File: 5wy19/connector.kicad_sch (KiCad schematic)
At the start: 1 part, among them J1 Conn_02x41_Row_Letter_First_S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

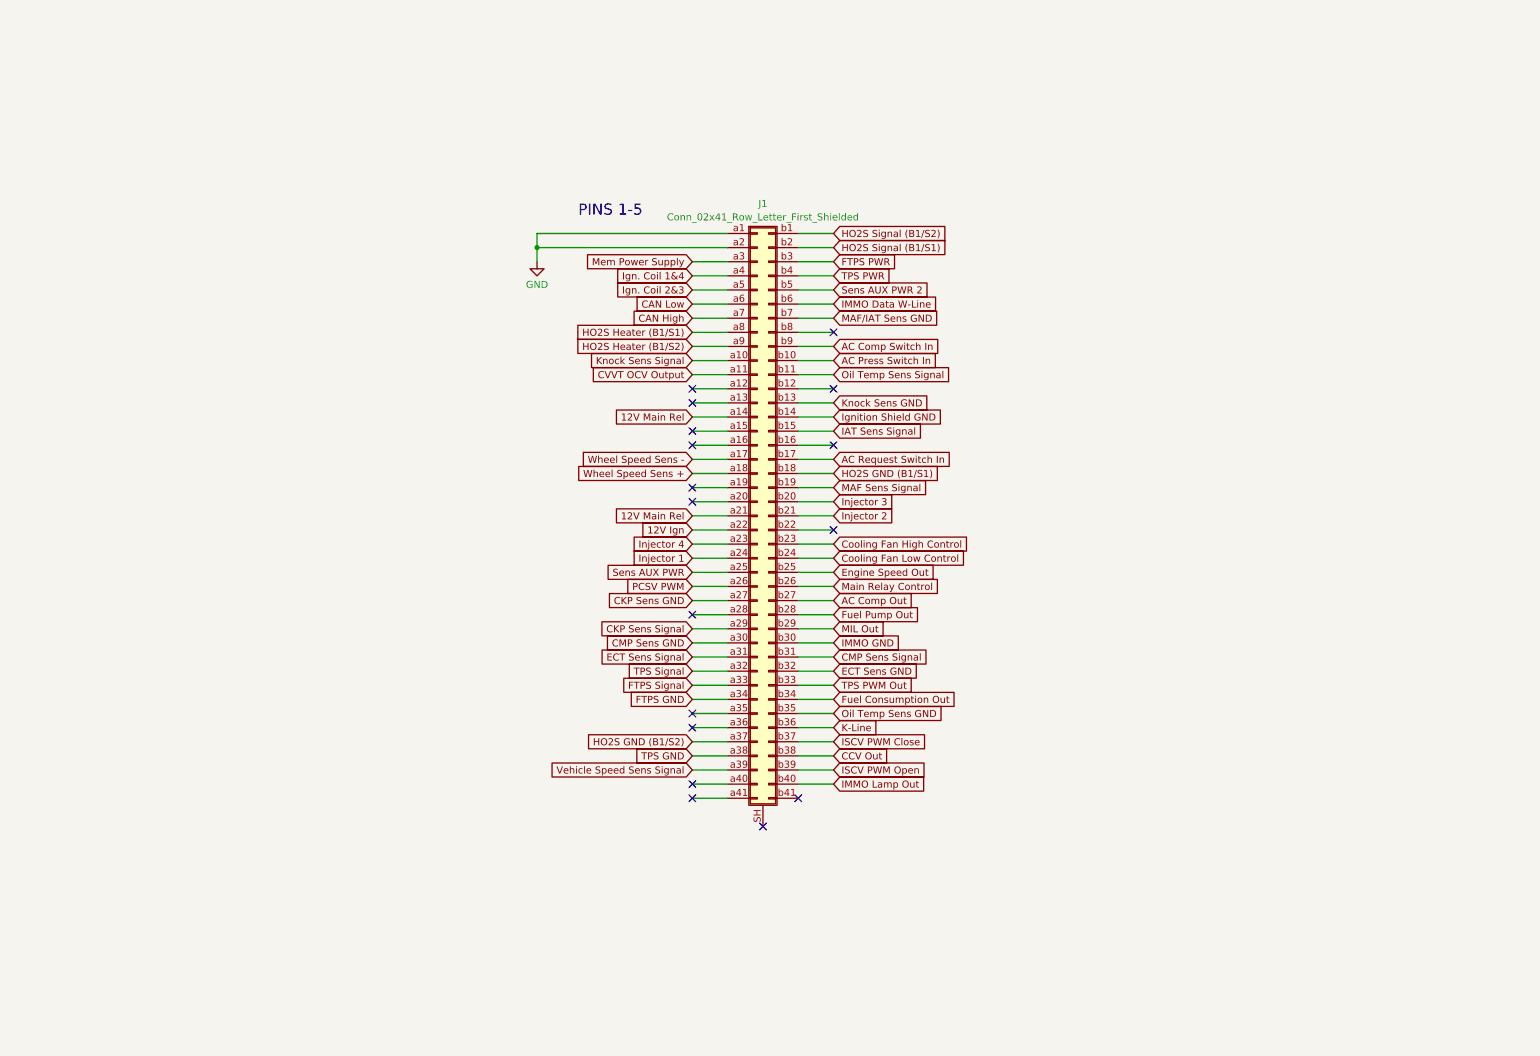
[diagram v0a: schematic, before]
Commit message: Finished most of the subsystems
-- MCU finished
-- Flash finished
-- Power Supply finished
-- I/O Drivers finished
-- CANBUS finished
-- Knock Control finished
-- Connector finished
-- Ignition Driver finished
-- Sensor Logic mostly finished
-- Logic ICs need some work
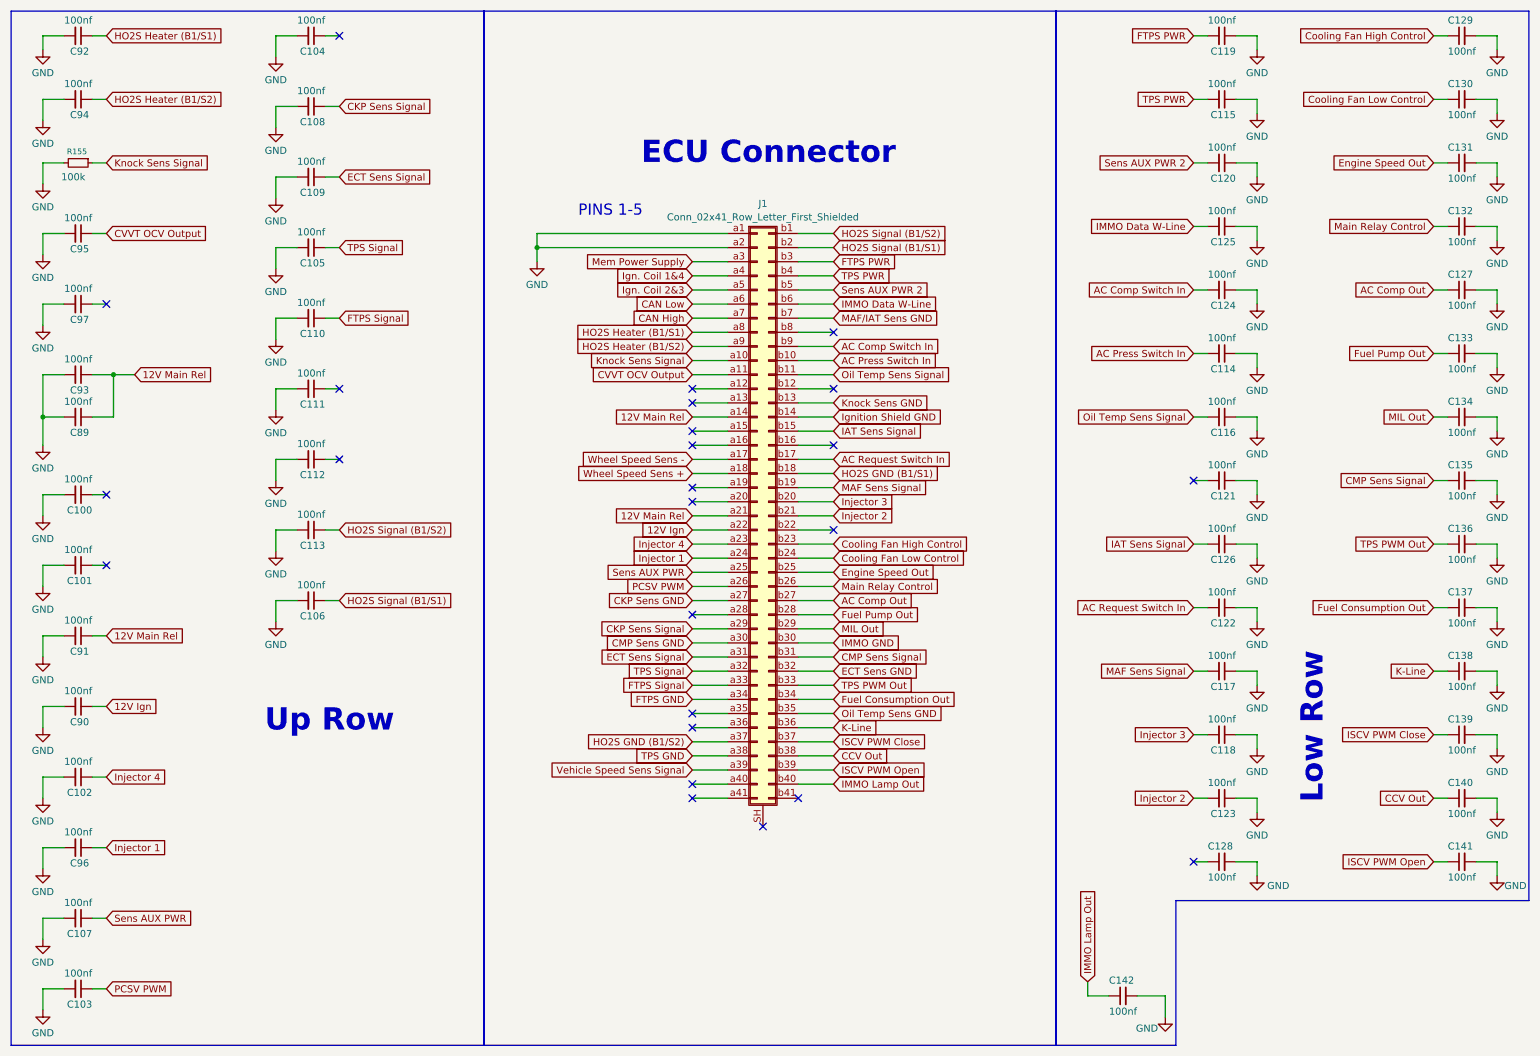
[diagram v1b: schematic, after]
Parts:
- added C100, C101, C102, C103, C104, C105, C106, C107, C108, C109, C110, C111, C112, C113, C114, C115, C116, C117, C118, C119, C120, C121, C122, C123, C124, C125, C126, C127, C128, C129, C130, C131, C132, C133, C134, C135, C136, C137, C138, C139, C140, C141, C142, C89, C90, C91, C92, C93, C94, C95, C96, C97: 100nf, symbol Device:C_Small
- added R155: 100k, symbol Device:R_Small
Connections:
- net 12V Ign: now also C90.1
- net 12V Main Rel: now also C89.1, C91.1, C93.1
- net AC Comp Out: now also C127.1
- net AC Comp Switch In: now also C124.2
- net AC Press Switch In: now also C114.2
- net AC Request Switch In: now also C122.2
- net CCV Out: now also C140.1
- net CKP Sens Signal: now also C108.1
- net CMP Sens Signal: now also C135.1
- net CVVT OCV Output: now also C95.1
- net Cooling Fan High Control: now also C129.1
- net Cooling Fan Low Control: now also C130.1
- net ECT Sens Signal: now also C109.1
- net Engine Speed Out: now also C131.1
- net FTPS PWR: now also C119.2
- net FTPS Signal: now also C110.1
- net Fuel Consumption Out: now also C137.1
- net Fuel Pump Out: now also C133.1
- net GND: now also C100.2, C101.2, C102.2, C103.2, C104.2, C105.2, C106.2, C107.2, C108.2, C109.2, C110.2, C111.2, C112.2, C113.2, C114.1, C115.1, C116.1, C117.1, C118.1, C119.1, C120.1, C121.1, C122.1, C123.1, C124.1, C125.1, C126.1, C127.2, C128.2, C129.2, C130.2, C131.2, C132.2, C133.2, C134.2, C135.2, C136.2, C137.2, C138.2, C139.2, C140.2, C141.2, C142.2, C89.2, C90.2, C91.2, C92.2, C93.2, C94.2, C95.2, C96.2, C97.2, R155.2
- net HO2S Heater (B1/S1): now also C92.1
- net HO2S Heater (B1/S2): now also C94.1
- net HO2S Signal (B1/S1): now also C106.1
- net HO2S Signal (B1/S2): now also C113.1
- net IAT Sens Signal: now also C126.2
- net IMMO Data W-Line: now also C125.2
- net IMMO Lamp Out: now also C142.1
- net ISCV PWM Close: now also C139.1
- net ISCV PWM Open: now also C141.1
- net Injector 1: now also C96.1
- net Injector 2: now also C123.2
- net Injector 3: now also C118.2
- net Injector 4: now also C102.1
- net K-Line: now also C138.1
- net Knock Sens Signal: now also R155.1
- net MAF Sens Signal: now also C117.2
- net MIL Out: now also C134.1
- net Main Relay Control: now also C132.1
- net Oil Temp Sens Signal: now also C116.2
- net PCSV PWM: now also C103.1
- net Sens AUX PWR: now also C107.1
- net Sens AUX PWR 2: now also C120.2
- net TPS PWM Out: now also C136.1
- net TPS PWR: now also C115.2
- net TPS Signal: now also C105.1
- no-connect marks 17 -> 25
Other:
- note added: "ECU Connector"
- note added: "Low Row"
- note added: "Up Row"
- title: (none) -> SMIK43 5WY19 Rev. Eng

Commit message: Final schematic (except maybe some oversights)
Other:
- note added: "Down Row"
- note removed: "Low Row"
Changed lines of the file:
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@@
 		)
 	)
-	(text "Low Row"
+	(text "Down Row"
 		(exclude_from_sim no)
 		(at 246.126 140.97 90)
